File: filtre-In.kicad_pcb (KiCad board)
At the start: 2 copper layers, 114 parts, among them P1 BNC Output, P10 BNC, P11 BNC, P12 BNC, P13 BNC, P14 BNC, P16 CONN_01X05, P17 CONN_01X01, P18 CONN_01X01, P19 CONN_01X01, P2 BNC Input, P20 CONN_01X01, P3 CONN_01X08, P4 CONN_01X01, P5 CONN_01X01, P6 CONN_01X01, P7 CONN_01X01, P9 BNC

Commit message: version avec formes 3D, sans condos ATC
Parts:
- R1: footprint Resistors_ThroughHole:R_Axial_DIN0411_L9.9mm_D3.6mm_P12.70mm_Horizontal -> Resistors_ThroughHole:Resistor_Horizontal_RM10mm
- moved D10 37.0 mm to (144.8, 59.7), turned to 0 degrees
- moved D11 37.0 mm to (130.8, 94.0), turned to 90 degrees
- moved D12 37.0 mm to (172.7, 59.7), turned to 0 degrees
- moved D13 37.0 mm to (158.8, 94.0), turned to 90 degrees
- moved D14 37.0 mm to (198.1, 59.7), turned to 0 degrees
- moved D15 37.0 mm to (184.2, 94.0), turned to 90 degrees
- moved D16 37.0 mm to (223.5, 59.7), turned to 0 degrees
- moved D17 37.0 mm to (209.6, 94.0), turned to 90 degrees
- moved D18 37.0 mm to (248.9, 59.7), turned to 0 degrees
- moved D19 37.0 mm to (234.9, 94.0), turned to 90 degrees
- moved D20 37.0 mm to (274.3, 59.7), turned to 0 degrees
- moved D21 37.0 mm to (260.4, 94.0), turned to 90 degrees
- moved P11 15.2 mm to (144.8, 120.7), turned to 315 degrees
- moved P14 15.2 mm to (160.0, 120.7), turned to 225 degrees
- moved L2 0.63 mm to (57.8, 44.5)
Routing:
- net Net-(C28-Pad2): track 173.0 -> 177.9 mm
- net Net-(C30-Pad2): track 81.9 -> 86.7 mm
- net Net-(P3-Pad8): track 15.8 -> 18.3 mm

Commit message: version CAO finale, a priori bonne pour la prod
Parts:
- added C42: C_Small, Capacitors_SMD:C_1825_HandSoldering, B.Cu at (35.6, 87.6)
- added C45: C_Small, Capacitors_SMD:C_1825_HandSoldering, B.Cu at (40.6, 78.7)
- added C46: C_Small, Capacitors_SMD:C_1825_HandSoldering, B.Cu at (61.0, 87.6)
- added C47: C_Small, Capacitors_SMD:C_1825_HandSoldering, B.Cu at (66.0, 78.7)
- added C48: C_Small, Capacitors_SMD:C_1825_HandSoldering, B.Cu at (86.4, 87.6)
- added C49: C_Small, Capacitors_SMD:C_1825_HandSoldering, B.Cu at (91.4, 78.7)
- added C50: C_Small, Capacitors_SMD:C_1825_HandSoldering, B.Cu at (111.8, 87.6)
- added C51: C_Small, Capacitors_SMD:C_1825_HandSoldering, B.Cu at (116.8, 78.7)
- added C52: C_Small, Capacitors_SMD:C_1825_HandSoldering, B.Cu at (137.2, 87.6)
- added C53: C_Small, Capacitors_SMD:C_1825_HandSoldering, B.Cu at (142.2, 78.7)
- added C54: C_Small, Capacitors_SMD:C_1825_HandSoldering, B.Cu at (165.1, 87.6)
- added C55: C_Small, Capacitors_SMD:C_1825_HandSoldering, B.Cu at (170.2, 78.7)
- added C56: C_Small, Capacitors_SMD:C_1825_HandSoldering, B.Cu at (190.5, 87.6)
- added C57: C_Small, Capacitors_SMD:C_1825_HandSoldering, B.Cu at (195.6, 78.7)
- added C58: C_Small, Capacitors_SMD:C_1825_HandSoldering, B.Cu at (215.9, 87.6)
- added C59: C_Small, Capacitors_SMD:C_1825_HandSoldering, B.Cu at (221.0, 78.7)
- added C60: C_Small, Capacitors_SMD:C_1825_HandSoldering, B.Cu at (241.3, 87.6)
- added C61: C_Small, Capacitors_SMD:C_1825_HandSoldering, B.Cu at (246.4, 78.7)
- added C62: C_Small, Capacitors_SMD:C_1825_HandSoldering, B.Cu at (266.7, 87.6)
- added C63: C_Small, Capacitors_SMD:C_1825_HandSoldering, B.Cu at (271.8, 78.7)
- R1: footprint Resistors_ThroughHole:Resistor_Horizontal_RM10mm -> Resistors_THT:R_Axial_DIN0411_L9.9mm_D3.6mm_P12.70mm_Horizontal
- moved C24 47.1 mm to (52.1, 100.3), turned to 0 degrees
- moved C35 47.1 mm to (63.5, 54.6), turned to 180 degrees
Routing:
- net GND: track 1203.3 -> 950.8 mm, vias 141 -> 104
- net Net-(C19-Pad1): track 29.9 -> 36.6 mm
- net Net-(C50-Pad2): track 29.9 -> 36.6 mm
- net Net-(C2-Pad1): track 29.9 -> 36.6 mm
- net Net-(C48-Pad2): track 29.9 -> 36.6 mm
- net Net-(C46-Pad2): track 29.9 -> 36.6 mm
- net Net-(C21-Pad1): track 29.9 -> 36.6 mm
- net Net-(C17-Pad1): track 29.9 -> 36.6 mm
- net Net-(C15-Pad1): track 29.9 -> 36.6 mm
- net Net-(C13-Pad1): track 29.9 -> 36.6 mm
- net Net-(C11-Pad1): track 29.9 -> 36.6 mm
- net Net-(C49-Pad2): track 24.8 -> 31.1 mm
- net Net-(C3-Pad1): track 24.8 -> 31.1 mm
- net Net-(C22-Pad1): track 24.8 -> 31.1 mm
- net Net-(C18-Pad1): track 24.8 -> 31.1 mm
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
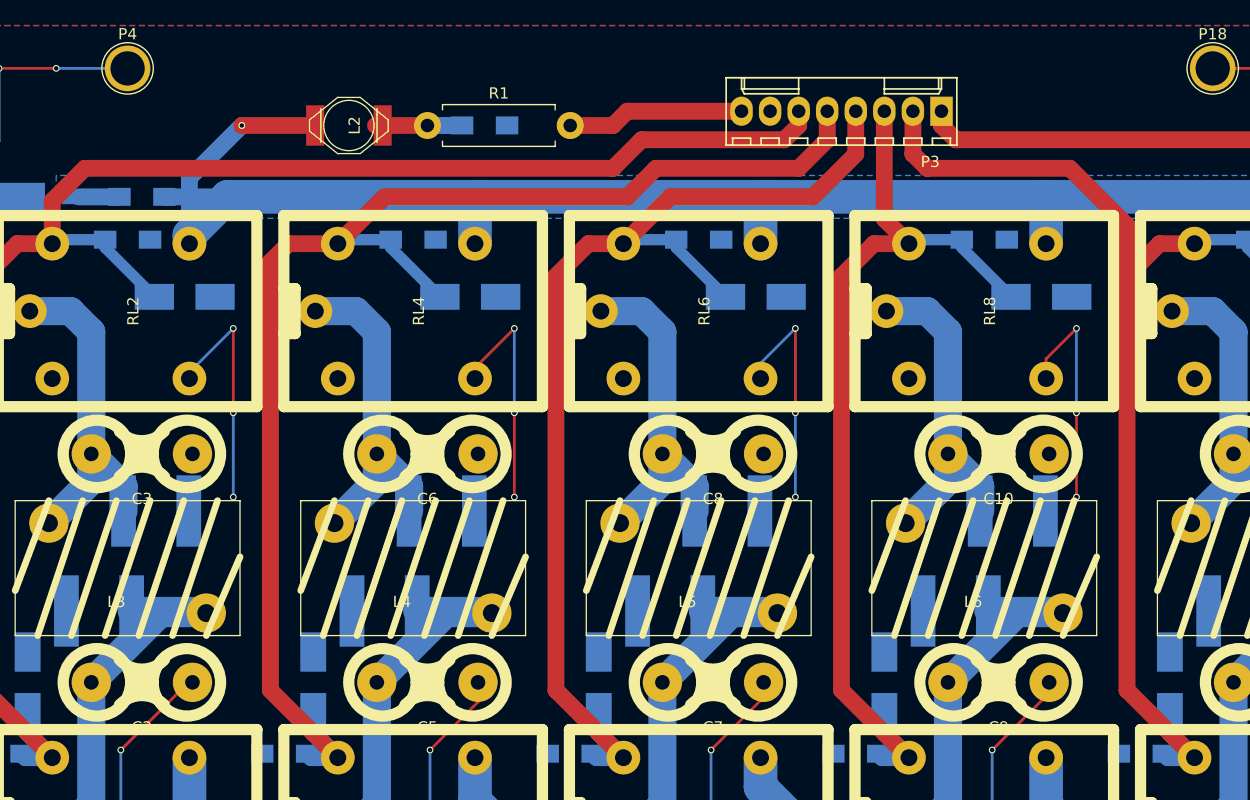
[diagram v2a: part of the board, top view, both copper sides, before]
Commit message: ajout gerber, modif bias
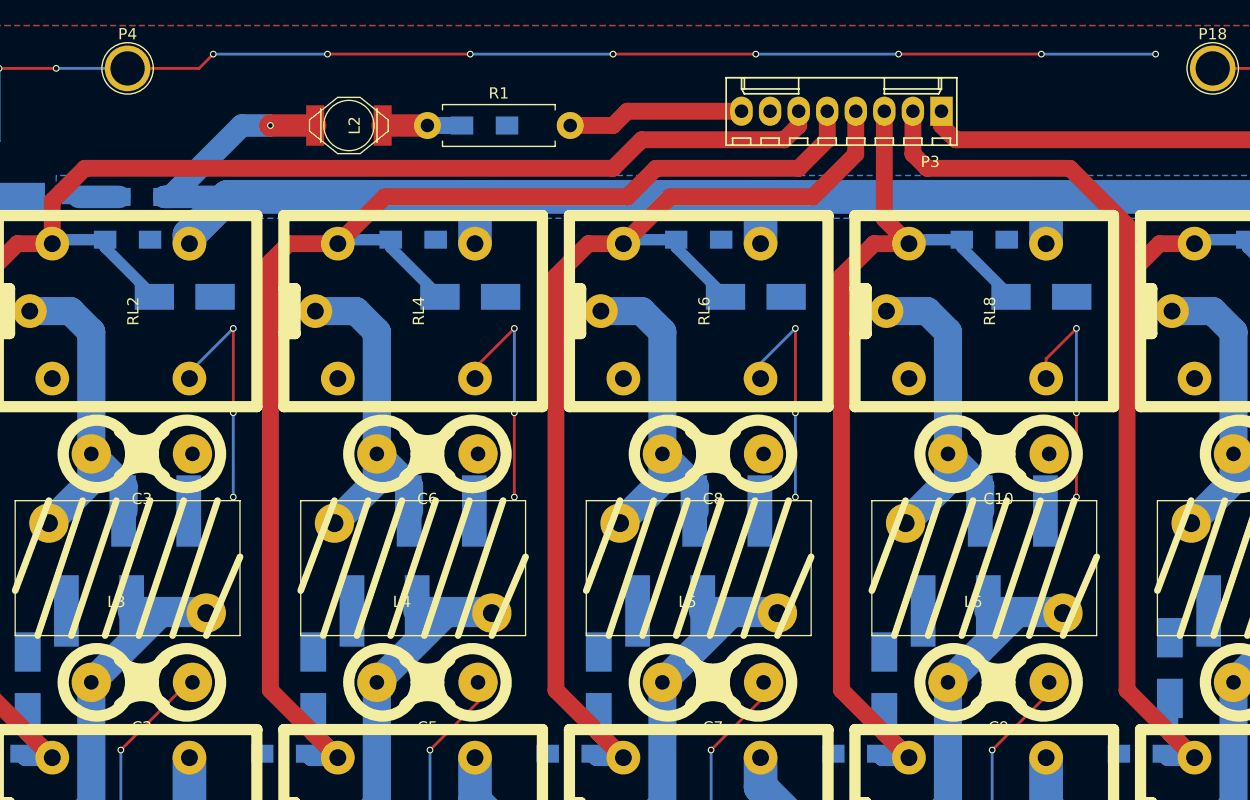
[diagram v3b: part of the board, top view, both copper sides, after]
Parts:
- moved D11 1.27 mm to (130.8, 92.7)
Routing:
- net GND: track 950.8 -> 1042.7 mm, vias 104 -> 112
- net Net-(C33-Pad1): track 324.5 -> 322.2 mm
- net Net-(C4-Pad2): track 7.70 -> 7.06 mm
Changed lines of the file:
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@@
     (thickness 1.6)
     (drawings 2)
-    (tracks 668)
+    (tracks 686)
     (zones 0)
     (modules 134)
@@
   )
   (setup
-    (last_trace_width 1.5)
+    (last_trace_width 0.25)
     (user_trace_width 1)
     (user_trace_width 1.5)
@@
     (visible_elements 7FFCFFFF)
     (pcbplotparams
-      (layerselection 0x00030_80000001)
+      (layerselection 0x010fc_80000001)
       (usegerberextensions false)
       (excludeedgelayer true)
@@
       (outputformat 1)
       (mirror false)
-      (drillshape 1)
+      (drillshape 0)
       (scaleselection 1)
-      (outputdirectory ""))
+      (outputdirectory C:/Users/Marco/Documents/Kicad/Projets/Filtre-Input/Gerber/))
   )
   (net 0 "")
@@
   )
   (module Diodes_SMD:D_SMB_Handsoldering (layer B.Cu)
-    (at 130.81 93.98 90)
+    (at 130.81 92.71 90)
     (descr "Diode SMB Handsoldering")
     (tags "Diode SMB Handsoldering")
@@
   (segment (start 45.1 87.82) (end 41.03 87.82) (width 2.5) (layer B.Cu) (net 3))
   (segment (start 33.02 106.68) (end 29.4 106.68) (width 2.5) (layer B.Cu) (net 3))
+  (segment (start 38.1 39.37) (end 44.45 39.37) (width 0.25) (layer F.Cu) (net 4))
+  (via (at 129.54 38.1) (size 0.6) (drill 0.4) (layers F.Cu B.Cu) (net 4))
+  (segment (start 119.38 38.1) (end 129.54 38.1) (width 0.25) (layer B.Cu) (net 4))
+  (via (at 119.38 38.1) (size 0.6) (drill 0.4) (layers F.Cu B.Cu) (net 4))
+  (segment (start 106.68 38.1) (end 119.38 38.1) (width 0.25) (layer F.Cu) (net 4))
+  (via (at 106.68 38.1) (size 0.6) (drill 0.4) (layers F.Cu B.Cu) (net 4))
+  (segment (start 93.98 38.1) (end 106.68 38.1) (width 0.25) (layer B.Cu) (net 4))
+  (via (at 93.98 38.1) (size 0.6) (drill 0.4) (layers F.Cu B.Cu) (net 4))
+  (segment (start 81.28 38.1) (end 93.98 38.1) (width 0.25) (layer F.Cu) (net 4))
+  (via (at 81.28 38.1) (size 0.6) (drill 0.4) (layers F.Cu B.Cu) (net 4))
+  (segment (start 68.58 38.1) (end 81.28 38.1) (width 0.25) (layer B.Cu) (net 4))
+  (via (at 68.58 38.1) (size 0.6) (drill 0.4) (layers F.Cu B.Cu) (net 4))
+  (segment (start 55.88 38.1) (end 68.58 38.1) (width 0.25) (layer F.Cu) (net 4))
+  (via (at 55.88 38.1) (size 0.6) (drill 0.4) (layers F.Cu B.Cu) (net 4))
+  (segment (start 45.72 38.1) (end 55.88 38.1) (width 0.25) (layer B.Cu) (net 4))
+  (via (at 45.72 38.1) (size 0.6) (drill 0.4) (layers F.Cu B.Cu) (net 4))
+  (segment (start 44.45 39.37) (end 45.72 38.1) (width 0.25) (layer F.Cu) (net 4))
   (segment (start 275.01 93.98) (end 275.01 94.99) (width 0.25) (layer B.Cu) (net 4))
   (segment (start 275.01 94.99) (end 270 100) (width 0.25) (layer B.Cu) (net 4))
@@
   (segment (start 33.02 60.96) (end 29.4 60.96) (width 2.5) (layer B.Cu) (net 5))
   (segment (start 34.87 62.81) (end 33.02 60.96) (width 2.5) (layer B.Cu) (net 5))
+  (segment (start 64.77 44.45) (end 60.785 44.45) (width 2) (layer F.Cu) (net 6))
   (segment (start 67.85 44.45) (end 64.77 44.45) (width 1.5) (layer B.Cu) (net 6))
-  (segment (start 64.77 44.45) (end 60.15 44.45) (width 1.5) (layer F.Cu) (net 6))
   (segment (start 113.94 78.74) (end 113.94 76.53) (width 2.5) (layer B.Cu) (net 7))
   (segment (start 113.94 76.53) (end 111.07 73.66) (width 2.5) (layer B.Cu) (net 7))
@@
   (segment (start 256.54 57.85) (end 256.54 94.68) (width 1.5) (layer F.Cu) (net 29))
   (segment (start 259.43 54.96) (end 256.54 57.85) (width 1.5) (layer F.Cu) (net 29))
-  (segment (start 54.15 44.45) (end 48.26 44.45) (width 1.5) (layer F.Cu) (net 30))
-  (via (at 48.26 44.45) (size 0.6) (drill 0.4) (layers F.Cu B.Cu) (net 30))
-  (segment (start 48.26 44.45) (end 43.6 49.11) (width 1.5) (layer B.Cu) (net 30))
-  (segment (start 43.6 49.11) (end 43.6 54.96) (width 1.5) (layer B.Cu) (net 30))
+  (via (at 50.8 44.45) (size 0.6) (drill 0.4) (layers F.Cu B.Cu) (net 30))
+  (segment (start 50.8 44.45) (end 48.26 44.45) (width 2) (layer B.Cu) (net 30))
+  (segment (start 41.37 50.8) (end 46.99 50.8) (width 2) (layer B.Cu) (net 30))
+  (segment (start 54.785 44.45) (end 50.8 44.45) (width 2) (layer F.Cu) (net 30))
+  (segment (start 48.26 44.45) (end 41.91 50.8) (width 2) (layer B.Cu) (net 30))
+  (segment (start 41.91 50.8) (end 41.37 50.8) (width 2) (layer B.Cu) (net 30))
   (segment (start 274.86 50.8) (end 273.05 50.8) (width 1.5) (layer B.Cu) (net 30))
-  (segment (start 41.37 50.8) (end 46.99 50.8) (width 1.5) (layer B.Cu) (net 30))
   (segment (start 161.434214 49.674214) (end 161.434214 50.655786) (width 1.5) (layer B.Cu) (net 30))
   (segment (start 161.434214 50.655786) (end 161.578428 50.8) (width 1.5) (layer B.Cu) (net 30))
@@
   (segment (start 273.05 50.8) (end 274.74 52.49) (width 3) (layer B.Cu) (net 30))
   (segment (start 274.74 52.49) (end 274.74 54.96) (width 3) (layer B.Cu) (net 30))
-  (segment (start 33.75 50.8) (end 37.37 50.8) (width 1.5) (layer B.Cu) (net 31))
+  (segment (start 37.37 50.8) (end 33.75 50.8) (width 2) (layer B.Cu) (net 31))
   (segment (start 92.71 43.18) (end 82.55 43.18) (width 1.5) (layer F.Cu) (net 32))
   (segment (start 81.28 44.45) (end 77.47 44.45) (width 1.5) (layer F.Cu) (net 32))

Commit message: version finale gravee
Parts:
- renumbered P4 to ?, P5 to ?, P6 to ?, P7 to ?, P17 to ?, P18 to ?, P19 to ?, P20 to ?
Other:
- board outline added: 263 x 92 mm
- board text added: "Design f6itu/f1fly"

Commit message: release from June 12 2017, debugged and checked
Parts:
- L1: moved to F.Cu
- P16: footprint Connectors_Molex:Molex_KK-6410-05_05x2.54mm_Straight -> conn_kk100:kk100_22-23-2051
- P3: footprint Connectors_Molex:Molex_KK-6410-08_08x2.54mm_Straight -> conn_kk100:kk100_22-23-2081
- moved D11 21.0 mm to (144.0, 109.0), turned to 0 degrees
- moved D13 20.7 mm to (173.0, 109.0), turned to 0 degrees
- moved D10 20.6 mm to (127.0, 70.0), turned to 270 degrees
- moved L1 20.5 mm to (54.0, 123.0)
- moved D15 20.4 mm to (198.0, 109.0), turned to 0 degrees
- moved D2 20.4 mm to (43.0, 109.0), turned to 0 degrees
- moved D21 20.3 mm to (274.0, 109.0), turned to 0 degrees
- moved D7 20.2 mm to (102.0, 70.0), turned to 270 degrees
- moved D17 20.2 mm to (223.0, 109.0), turned to 0 degrees
- moved D20 20.2 mm to (257.0, 70.0), turned to 270 degrees
- moved D4 20.1 mm to (68.0, 109.0), turned to 0 degrees
- moved D19 19.9 mm to (248.0, 109.0), turned to 0 degrees
- moved D5 19.9 mm to (77.0, 70.0), turned to 270 degrees
- moved D6 19.9 mm to (93.0, 109.0), turned to 0 degrees
- moved D8 19.6 mm to (118.0, 109.0), turned to 0 degrees
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- gave numbers to parts that had none: 8
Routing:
- net GND: track 1042.7 -> 476.0 mm, vias 112 -> 42
- net Net-(C1-Pad1): track 473.0 -> 317.6 mm
- net Net-(C33-Pad1): track 322.2 -> 440.5 mm
- net Net-(C23-Pad2): track 146.3 -> 178.6 mm
- net Net-(C25-Pad2): track 99.8 -> 127.4 mm
- net Net-(C24-Pad2): track 122.7 -> 149.9 mm
- net Net-(C26-Pad2): track 84.7 -> 107.7 mm
- net Net-(C31-Pad2): track 105.1 -> 123.8 mm
- net Net-(C29-Pad2): track 105.8 -> 124.3 mm
- net Net-(C28-Pad2): track 177.9 -> 196.2 mm
- net Net-(C32-Pad2): track 128.0 -> 145.9 mm
- net Net-(C27-Pad2): track 102.0 -> 119.5 mm
- net Net-(C30-Pad2): track 86.7 -> 103.3 mm
- net Net-(C14-Pad1): track 30.3 -> 32.3 mm
- net Net-(C48-Pad2): track 36.6 -> 38.3 mm
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
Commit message: changed relay pinout, changed ATC-B footprint
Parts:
- C42, C45, C46, C47, C48, C49, C50, C51, C52, C53, C54, C55, C56, C57, C58, C59, C60, C61, C62, C63: footprint Capacitors_SMD:C_1825_HandSoldering -> ATC_B:Capacitors_ATC_B_HandSoldering
- moved C52 4.66 mm to (132.5, 87.5)
- moved C50 4.26 mm to (107.5, 87.5)
- moved C62 4.20 mm to (262.5, 87.5)
- moved C48 3.86 mm to (82.5, 87.5)
- moved C60 3.80 mm to (237.5, 87.5)
- moved C46 3.46 mm to (57.5, 87.5)
- moved C58 3.40 mm to (212.5, 87.5)
- moved C42 3.06 mm to (32.5, 87.5)
- moved C56 3.00 mm to (187.5, 87.5)
- moved C54 2.60 mm to (162.5, 87.5)
- moved C63 1.93 mm to (270.0, 78.0)
- moved C45 1.80 mm to (39.0, 78.0)
- moved C57 1.74 mm to (194.0, 78.0)
- moved C49 1.62 mm to (90.0, 78.0)
- moved C61 1.57 mm to (245.0, 78.0)
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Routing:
- net Net-(C46-Pad2): track 37.9 -> 39.3 mm
- net Net-(C22-Pad1): track 30.4 -> 29.3 mm
- net Net-(C3-Pad1): track 31.1 -> 30.1 mm
- net Net-(C16-Pad1): track 31.1 -> 30.1 mm
- net Net-(C49-Pad2): track 31.5 -> 30.5 mm
- net Net-(C20-Pad1): track 31.4 -> 30.5 mm
- net Net-(C12-Pad1): track 32.4 -> 31.5 mm
- net Net-(C14-Pad1): track 32.3 -> 31.4 mm
- net Net-(C11-Pad1): track 38.1 -> 38.9 mm
- net Net-(C47-Pad2): track 31.3 -> 30.5 mm
- net Net-(C18-Pad1): track 31.3 -> 30.5 mm
- net Net-(C10-Pad1): track 32.2 -> 31.5 mm
- net Net-(C2-Pad1): track 37.1 -> 37.8 mm
- net Net-(C50-Pad2): track 38.2 -> 38.9 mm
- net Net-(C21-Pad1): track 37.9 -> 38.5 mm
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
